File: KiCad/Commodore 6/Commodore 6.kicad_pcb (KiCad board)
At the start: 4 copper layers, 127 x 127 mm, 125 parts, among them J1 472192001, J2 PPTC071LFBN-RC, J3 6130XX11121_61300511121, J4 Conn_01x02_Pin, J5 FTSH-107-01-L-DV-K-A, J6 M20-6112045, J7 FH12-24S-0.5SH_55_, J8 FH12-22S-0.5SH55, J9 Conn_01x06, Q1 NTR4501NT1G, Q2 PMOS, SW1 SLW-1277545-3A-RA-N-D, SW1A1 SLW-1277545-3A-RA-N-D, SW2 SLW-1277545-3A-RA-N-D, SW3 SLW-1277545-3A-RA-N-D, U1 STM32H562RIT6, U2 STM32H7A3RIT6, U3 SN65HVD74DR, U4 TS3A27518EIPWRQ1, U5 SN74CBT16233DLR, U6 TCA9509DGKR, U7 ADV7280AWBCPZ, U8 TLV1117LV33DCYR, Y1 ABM8AIG-28.63636MHZ

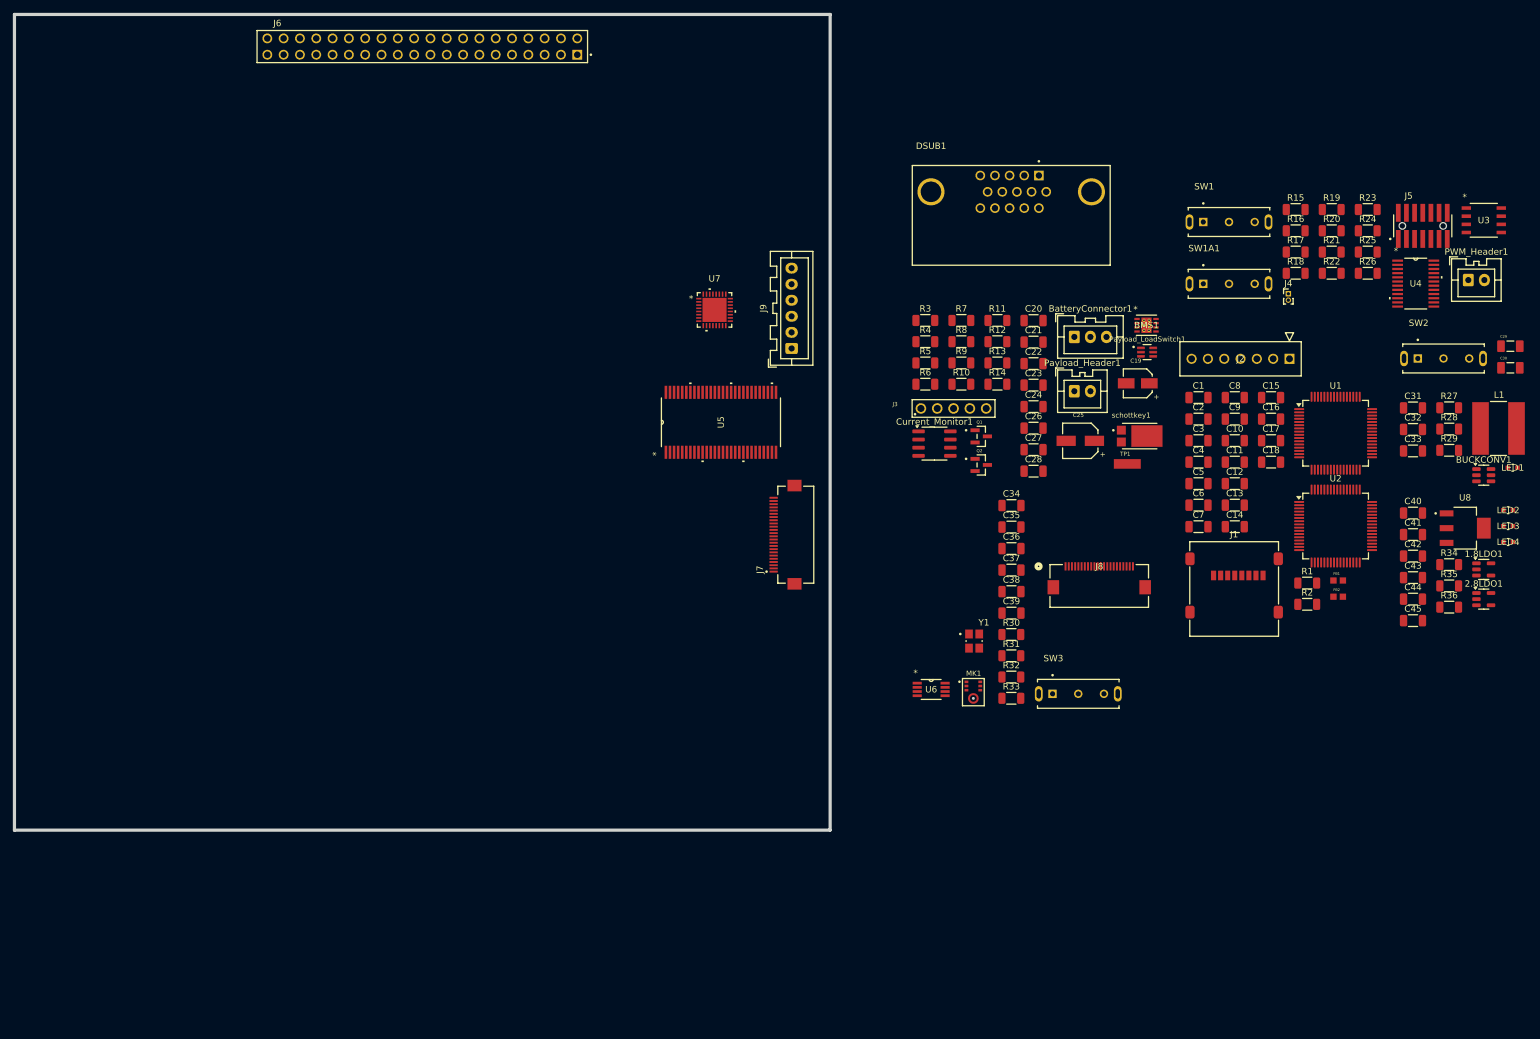
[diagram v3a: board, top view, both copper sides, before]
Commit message: Started Routing Camera stuff
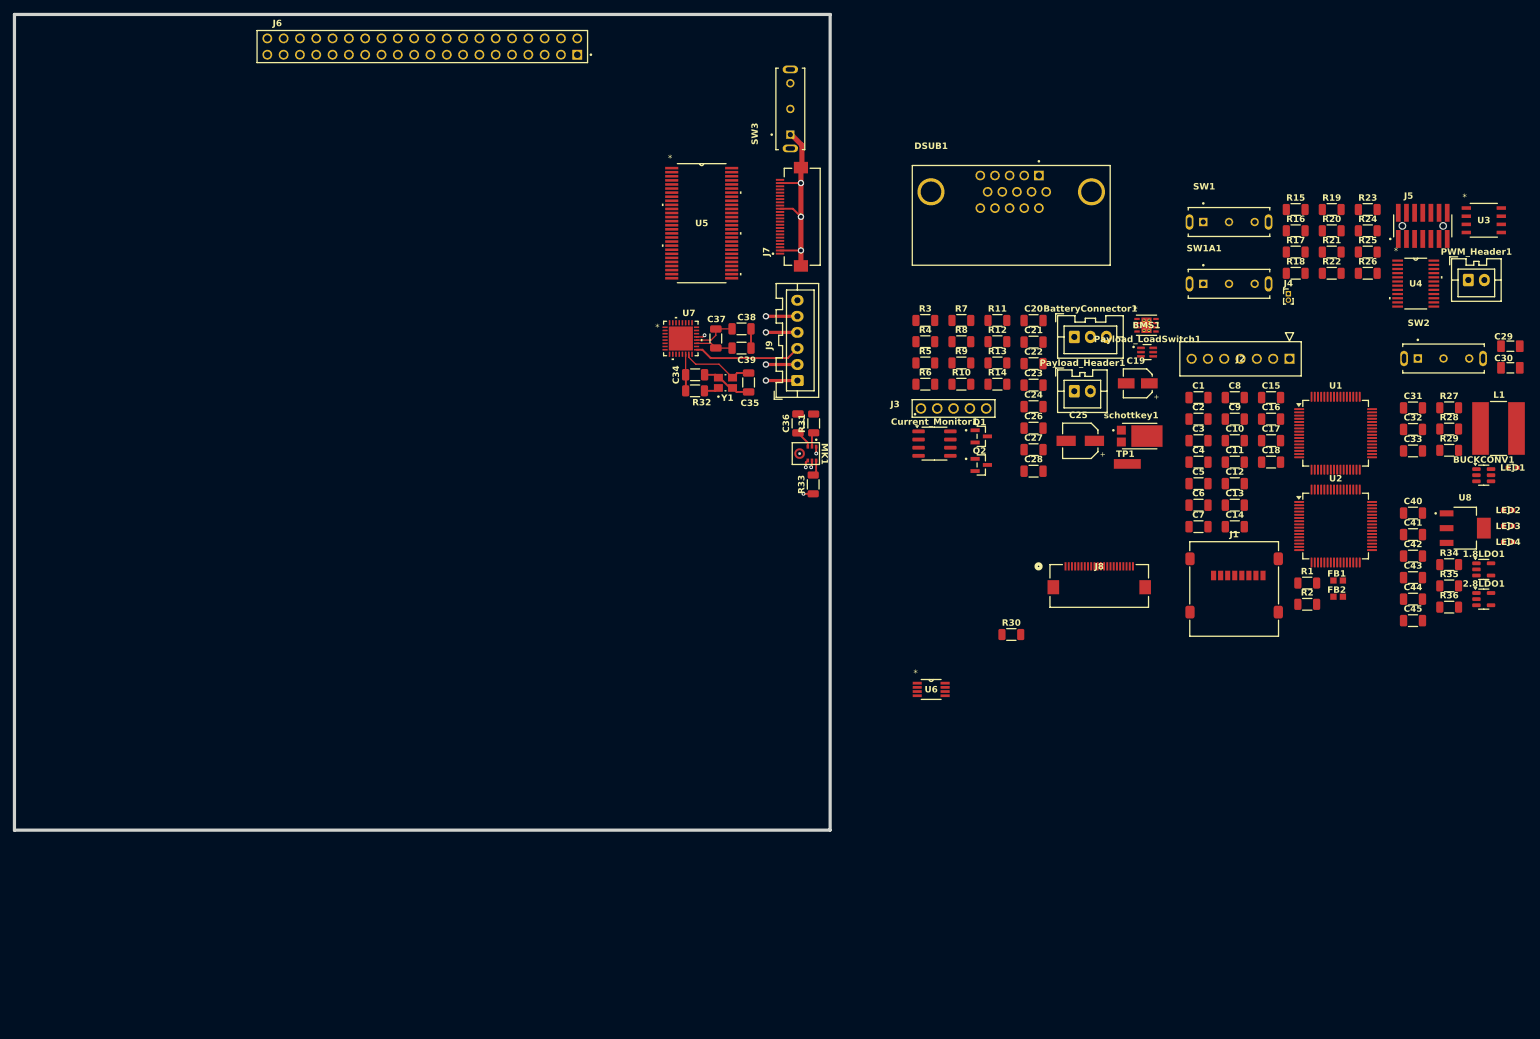
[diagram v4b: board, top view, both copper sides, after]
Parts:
- moved SW3 101.5 mm to (120.8, 14.7), turned to 90 degrees
- moved R32 66.4 mm to (106.0, 58.6)
- moved C39 58.9 mm to (113.2, 52.0), turned to 180 degrees
- moved C38 58.7 mm to (113.2, 49.0), turned to 180 degrees
- moved C37 58.5 mm to (109.2, 50.5), turned to -90 degrees
- moved Y1 55.8 mm to (110.7, 57.4), turned to 90 degrees
- moved C34 53.3 mm to (106.0, 56.1), turned to 180 degrees
- moved J7 49.5 mm to (122.0, 31.5)
- moved R31 47.5 mm to (124.4, 63.7), turned to 90 degrees
- moved C35 46.7 mm to (114.3, 57.3), turned to 90 degrees
- moved R33 45.4 mm to (124.4, 73.2), turned to 90 degrees
- moved MK1 45.3 mm to (123.2, 68.4), turned to -90 degrees
- moved C36 38.5 mm to (122.0, 63.7), turned to 90 degrees
- moved U5 31.1 mm to (107.0, 32.5), turned to 0 degrees
- moved U7 6.88 mm to (103.8, 50.5)
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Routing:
- net GNDA: track 0.00 -> 47.5 mm, vias 0 -> 4
- net /STM32/Camera/CAM_NTSC: track 0.00 -> 16.9 mm
- net Net-(U7-XTALN): track 0.00 -> 11.4 mm
- net Net-(U7-VREFN): track 0.00 -> 6.86 mm
- net Net-(U7-VREFP): track 0.00 -> 5.87 mm
- net Net-(U7-XTALP): track 0.00 -> 5.72 mm
- net CAM_RX: track 0.00 -> 4.90 mm, vias 0 -> 1
- net +5V: track 0.00 -> 4.90 mm, vias 0 -> 1
- net CAM_TX: track 0.00 -> 4.90 mm, vias 0 -> 1
- net Net-(MK1-VDD): track 0.00 -> 2.78 mm
- net Net-(MK1-SD): track 0.00 -> 2.45 mm
- net Net-(R32-Pad2): track 0.00 -> 2.32 mm
- net Net-(MK1-CONFIG): track 0.00 -> 2.27 mm
- net I2S_SD: track 0.00 -> 1.51 mm, vias 0 -> 1
- net 1.8V: track 0.00 -> 1.35 mm, vias 0 -> 1
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
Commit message: Tried to route DCMI and started SWD connector
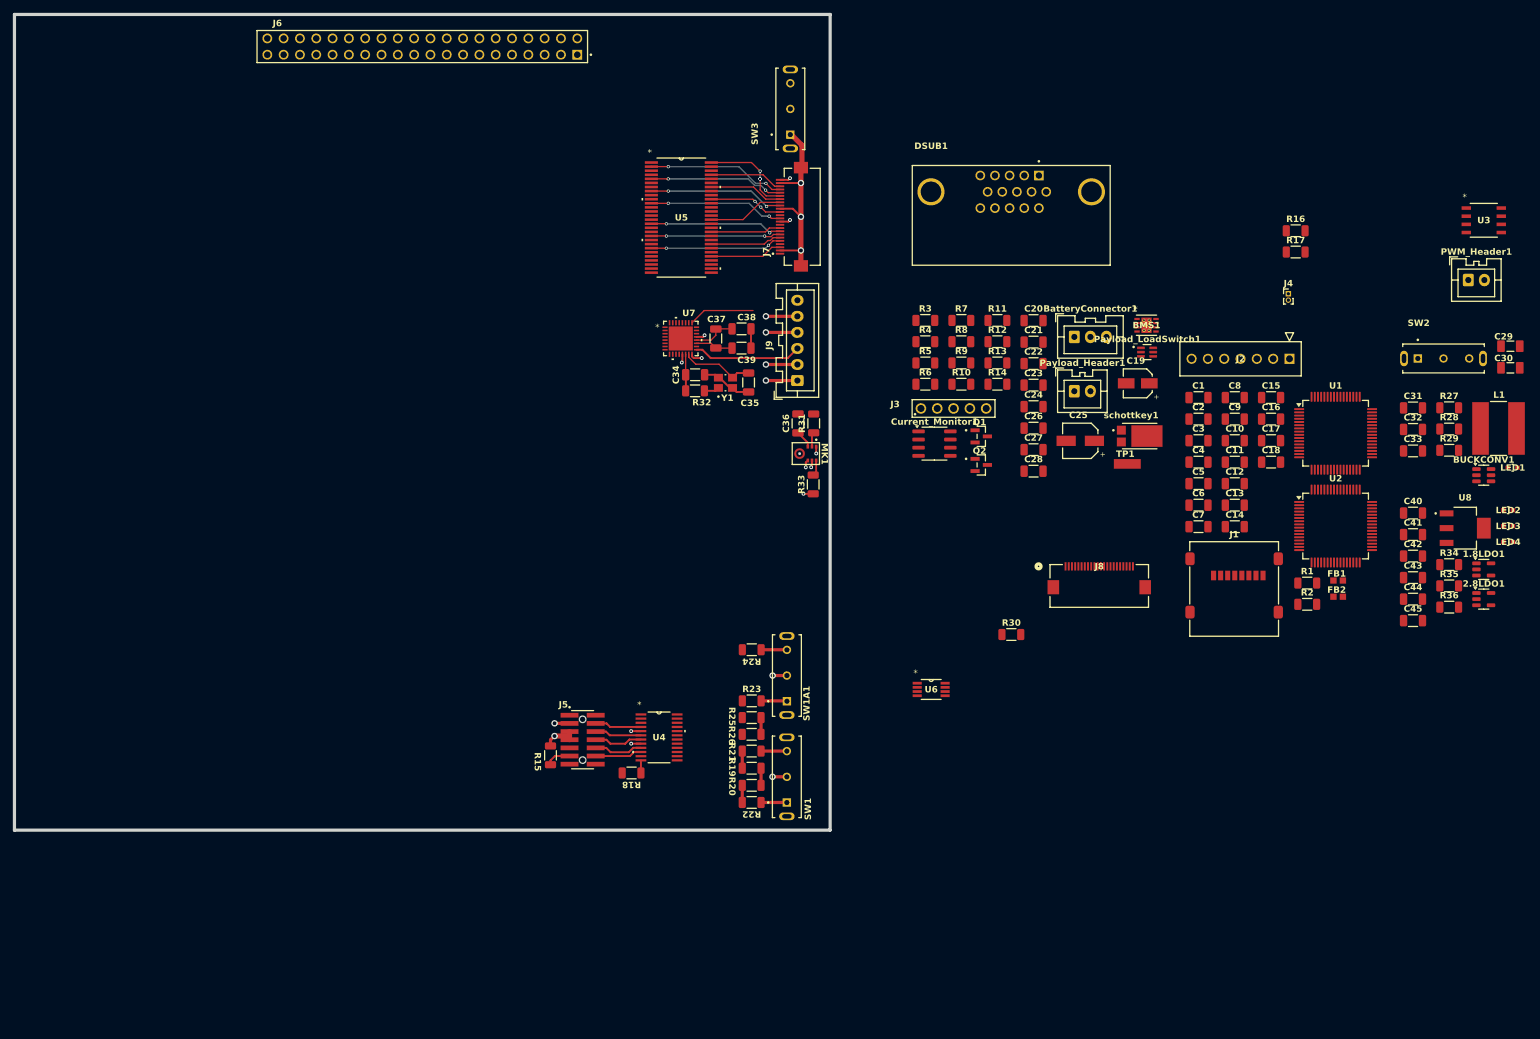
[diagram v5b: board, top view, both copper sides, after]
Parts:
- moved J5 153.3 mm to (88.5, 112.9), turned to -90 degrees
- moved R15 143.8 mm to (83.5, 115.3), turned to -90 degrees
- moved U4 137.4 mm to (100.4, 112.6)
- moved R18 129.4 mm to (96.1, 118.1), turned to 180 degrees
- moved R19 125.4 mm to (114.8, 117.4), turned to 180 degrees
- moved R20 124.9 mm to (114.8, 120.0)
- moved R23 122.7 mm to (114.8, 106.9)
- moved R22 122.2 mm to (114.8, 122.7), turned to 180 degrees
- moved R25 120.2 mm to (114.8, 109.5), turned to 180 degrees
- moved R26 119.8 mm to (114.8, 112.1), turned to 180 degrees
- moved R21 119.1 mm to (114.8, 114.7), turned to 180 degrees
- moved R24 116.0 mm to (114.8, 98.9), turned to 180 degrees
- moved SW1 110.5 mm to (120.3, 118.7), turned to 90 degrees
- moved SW1A1 92.0 mm to (120.3, 102.9), turned to 90 degrees
- moved U5 3.29 mm to (103.8, 31.6)
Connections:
- J5 pad 05: GNDA -> GNDD
- J5 pad 07: GNDA -> GNDD
- R15 pad 1: GNDA -> GNDD
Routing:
- net DCMI_D1: track 0.00 -> 21.6 mm, vias 0 -> 2
- net DCMI_D5: track 0.00 -> 21.1 mm, vias 0 -> 2
- net DCMI_D7: track 0.00 -> 21.0 mm, vias 0 -> 2
- net DCMI_D3: track 0.00 -> 20.9 mm, vias 0 -> 2
- net DCMI_PWDN: track 0.00 -> 20.7 mm, vias 0 -> 2
- net DCMI_SCL: track 0.00 -> 20.5 mm, vias 0 -> 2
- net DCMI_VSYNC: track 0.00 -> 20.2 mm, vias 0 -> 2
- net DCMI_D0: track 0.00 -> 14.6 mm, vias 0 -> 3
- net DCMI_PIXCLK: track 0.00 -> 11.8 mm
- net DCMI_D6: track 0.00 -> 11.5 mm, vias 0 -> 2
- net DCMI_D4: track 0.00 -> 11.5 mm
- net DCMI_D2: track 0.00 -> 11.4 mm
- net DCMI_SDA: track 0.00 -> 11.3 mm
- net DCMI_RST: track 0.00 -> 11.1 mm
- net DCMI_HSYNC: track 0.00 -> 10.9 mm
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
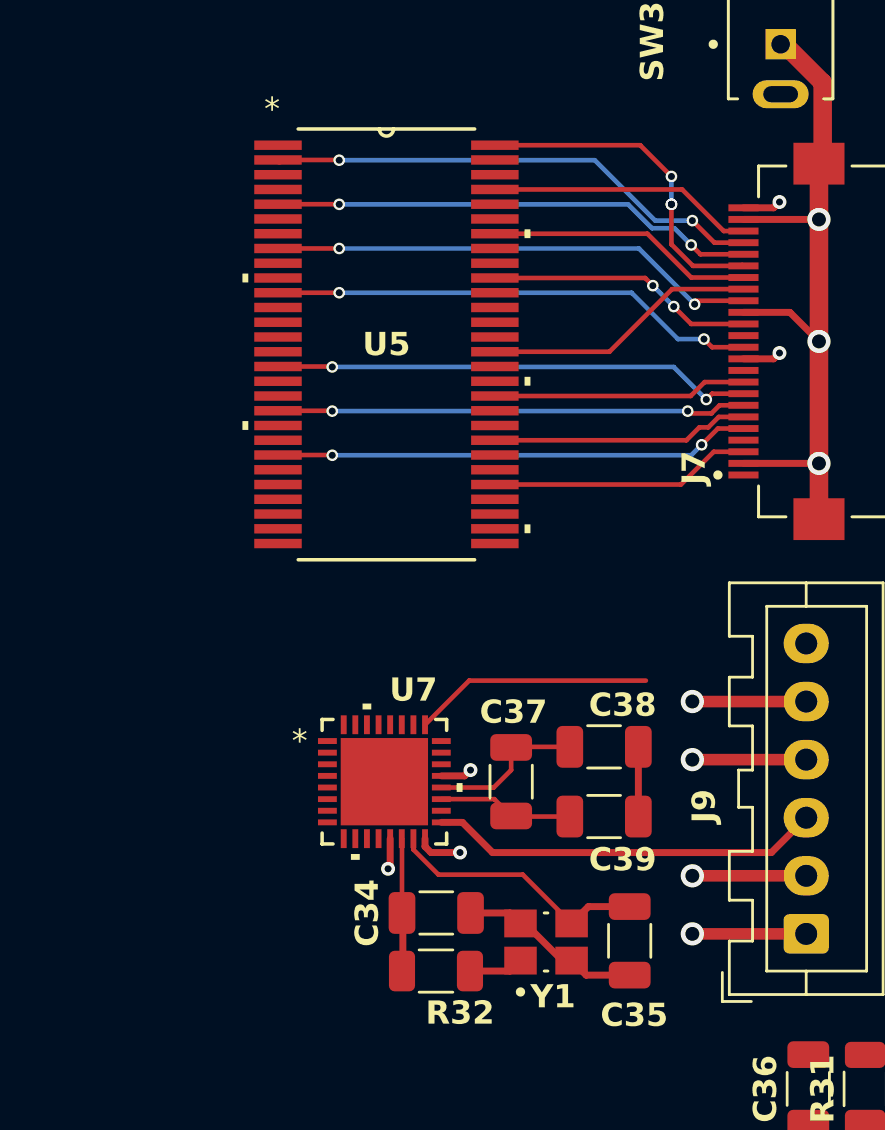
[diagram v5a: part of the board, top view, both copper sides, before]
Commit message: NTSR routed (Bad but routed)
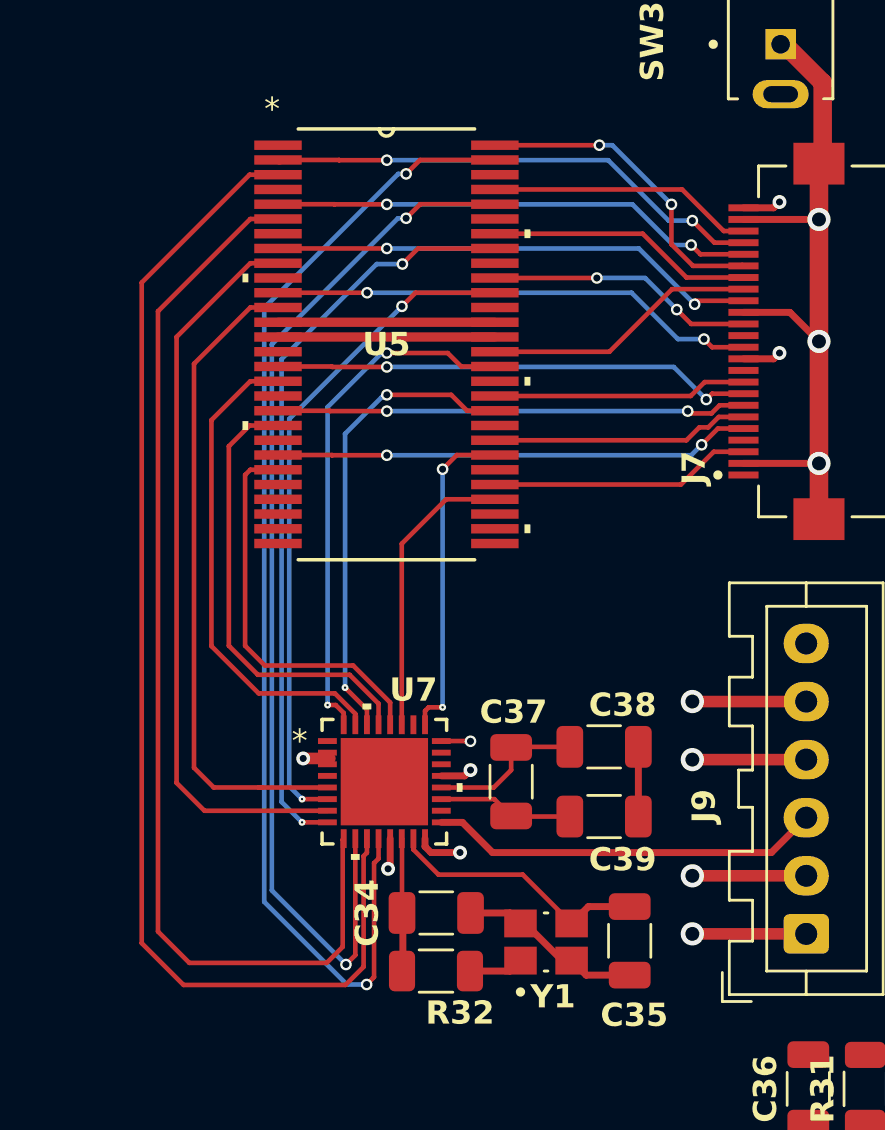
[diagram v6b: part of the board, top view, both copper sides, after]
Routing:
- net NTSC_D1: track 0.00 -> 52.4 mm
- net NTSC_D0: track 0.00 -> 50.5 mm, vias 0 -> 2
- net NTSC_D3: track 0.00 -> 47.0 mm
- net NTSC_D2: track 0.00 -> 45.7 mm, vias 0 -> 2
- net NTSC_D4: track 0.00 -> 32.5 mm, vias 0 -> 2
- net NTSC_D5: track 0.00 -> 31.9 mm
- net NTSC_D6: track 0.00 -> 28.8 mm, vias 0 -> 2
- net NTSC_D7: track 0.00 -> 28.3 mm
- net NTSC_PIXCLK: track 0.00 -> 22.6 mm, vias 0 -> 2
- net NTSC_PWDN: track 0.00 -> 21.2 mm
- net NTSC_HSYNC: track 0.00 -> 20.4 mm, vias 0 -> 2
- net NTSC_VSYNC: track 0.00 -> 19.5 mm
- net NTSC_SCL: track 0.00 -> 17.1 mm
- net NTSC_SDA: track 0.00 -> 12.6 mm
- net GNDA: track 54.3 -> 63.7 mm
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
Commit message: Figured out STM Placement
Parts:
- moved LED4 188.9 mm to (46.7, 116.0)
- moved R36 184.1 mm to (40.8, 116.0)
- moved C40 179.9 mm to (41.0, 111.0)
- moved U8 179.7 mm to (48.9, 111.0)
- moved FB1 166.8 mm to (50.0, 29.3)
- moved LED3 166.2 mm to (70.5, 116.5)
- moved C45 163.2 mm to (56.0, 116.0)
- moved R35 161.6 mm to (64.3, 117.0)
- moved 1.8LDO1 159.7 mm to (71.3, 113.0)
- moved J2 159.0 mm to (39.6, 60.0)
- moved DSUB1 158.8 mm to (18.0, 107.5)
- moved U1 158.1 mm to (50.0, 38.0), turned to -135 degrees
- moved C42 156.1 mm to (64.3, 113.0)
- moved LED2 146.9 mm to (91.1, 117.0)
- moved SW1 144.6 mm to (26.6, 8.48), turned to 180 degrees
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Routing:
- net NTSC_D3: track 47.0 -> 38.1 mm
- net NTSC_D1: track 52.4 -> 43.8 mm
- net NTSC_D2: track 45.7 -> 39.1 mm
- net NTSC_D0: track 50.5 -> 44.6 mm

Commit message: 0805
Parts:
- C1, C10, C11, C12, C13, C14, C15, C16, C17, C18, C2, C3, C4, C5, C6, C7, C8, C9: footprint Capacitor_SMD:C_1206_3216Metric -> Capacitor_SMD:C_0805_2012Metric
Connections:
- J5 pad 05: GNDD -> GNDA
- J5 pad 07: GNDD -> GNDA
- R15 pad 1: GNDD -> GNDA
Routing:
- net GNDD: track 5.36 -> 0.00 mm, vias 1 -> 0
- net GNDA: track 63.7 -> 69.0 mm, vias 5 -> 6
